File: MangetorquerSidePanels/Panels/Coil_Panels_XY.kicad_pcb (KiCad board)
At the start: 6 copper layers, 82 x 99 mm, 17 parts, among them J1 Through_Hole_1, J2 MOLEX_2053380006

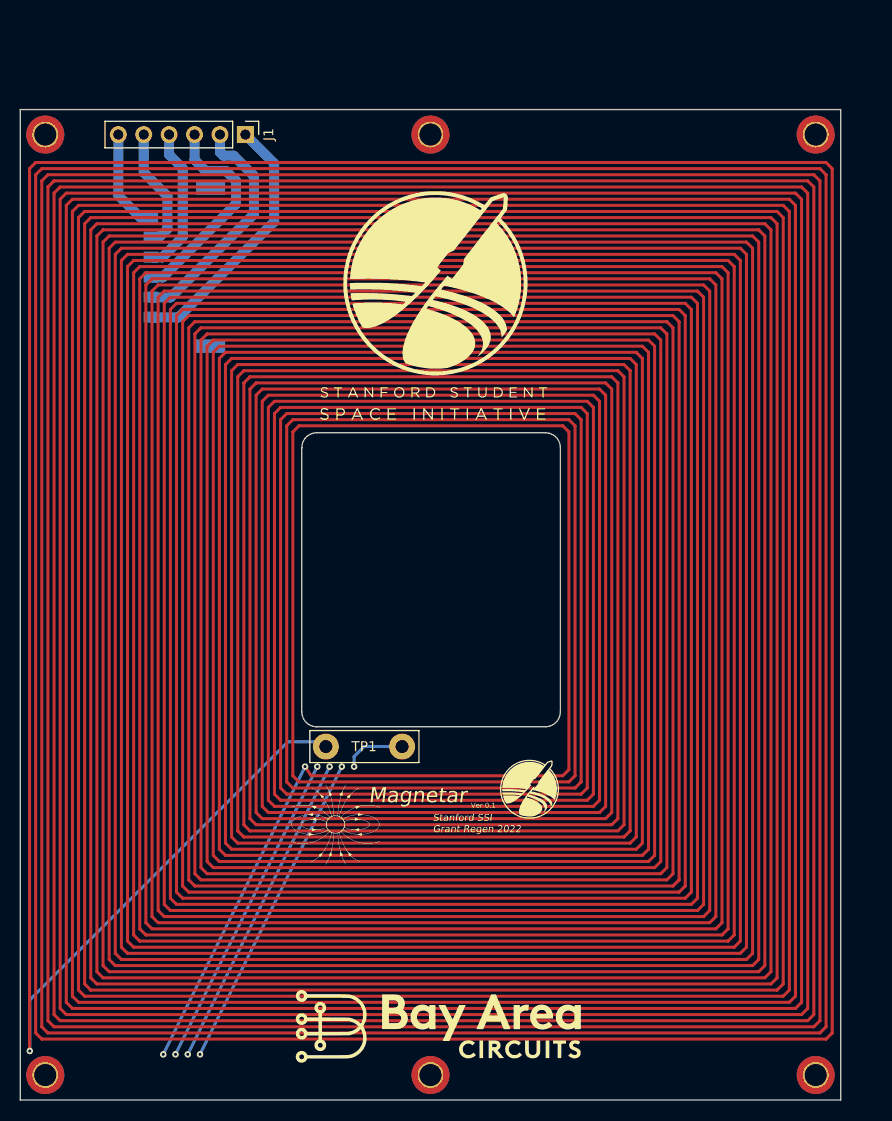
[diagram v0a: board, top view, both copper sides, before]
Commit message: Final flight side panels w/ magnetorquers finished, note final board thickness of 0.031'' and updated copper weight of 0.5oz for internal layers
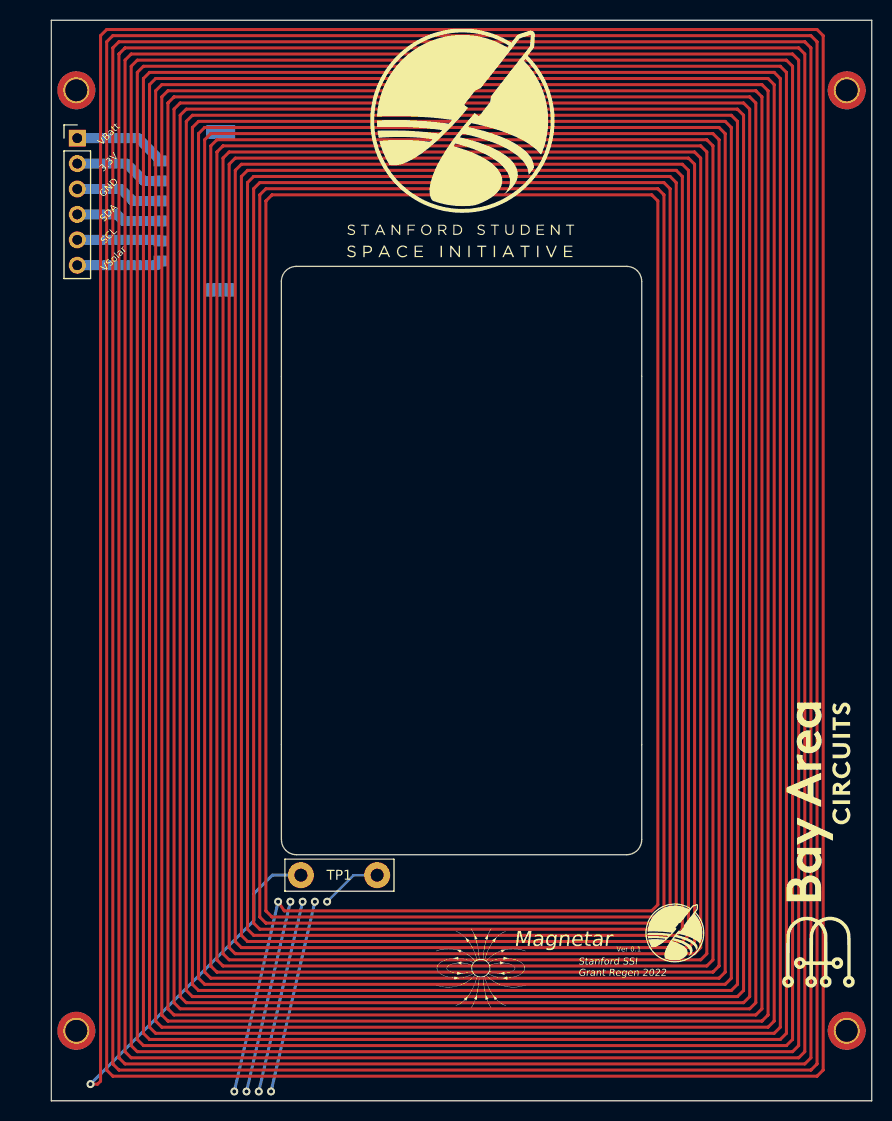
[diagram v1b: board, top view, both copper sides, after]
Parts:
- removed H5, H6: ~, MountingHole:MountingHole_2.2mm_M2_DIN965_Pad_TopBottom
- moved H2 98.8 mm to (192.0, 139.5)
- moved H4 98.5 mm to (115.0, 45.5)
- moved H1 89.6 mm to (115.0, 139.5)
- moved REF** 41.4 mm to (188.8, 120.7), turned to 90 degrees
- moved REF** 28.7 mm to (188.0, 130.5)
- moved REF** 28.7 mm to (168.7, 127.2)
- moved REF** 20.4 mm to (174.7, 130.0)
- moved REF** 20.4 mm to (155.5, 133.2)
- moved REF** 19.5 mm to (131.4, 137.0)
- moved J1 16.8 mm to (115.1, 50.3), turned to 0 degrees
- moved REF** 16.5 mm to (153.8, 49.2)
- moved REF** 15.9 mm to (153.4, 48.2)
- moved TP1 13.1 mm to (141.3, 124.4)
- moved J2 5.70 mm to (127.0, 57.6)
- moved H3 5.40 mm to (192.0, 45.5)
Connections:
- net Coil_OUT renamed Coil_IN
- J1 pad 1: Net-(J1-Pad1) -> Net-(J2-Pad1)
- J1 pad 2: Net-(J1-Pad2) -> Net-(J2-Pad2)
- J1 pad 3: Net-(J1-Pad3) -> Net-(J2-Pad3)
- J1 pad 4: Net-(J1-Pad4) -> Net-(J2-Pad4)
- J1 pad 5: Net-(J1-Pad5) -> Net-(J2-Pad5)
- J1 pad 6: Net-(J1-Pad6) -> Net-(J2-Pad6)
- J2 pad 1: Net-(J1-Pad6) -> Net-(J2-Pad1)
- J2 pad 2: Net-(J1-Pad5) -> Net-(J2-Pad2)
- J2 pad 3: Net-(J1-Pad4) -> Net-(J2-Pad3)
- J2 pad 4: Net-(J1-Pad3) -> Net-(J2-Pad4)
- J2 pad 5: Net-(J1-Pad2) -> Net-(J2-Pad5)
- J2 pad 6: Net-(J1-Pad1) -> Net-(J2-Pad6)
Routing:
- net Coil_IN: track 50604.5 -> 40226.0 mm
- net Net-(J1-Pad1): track 26.1 -> 0.00 mm
- net Net-(J1-Pad2): track 23.6 -> 0.00 mm
- net Net-(J1-Pad3): track 21.3 -> 0.00 mm
- net Net-(J1-Pad4): track 14.7 -> 0.00 mm
- net Net-(J1-Pad5): track 12.3 -> 0.00 mm
- net Net-(J1-Pad6): track 10.4 -> 0.00 mm
- net Net-(J2-Pad1): track 0.00 -> 9.30 mm
- net Net-(J2-Pad2): track 0.00 -> 9.08 mm
- net Net-(J2-Pad3): track 0.00 -> 8.86 mm
- net Net-(J2-Pad4): track 0.00 -> 8.63 mm
- net Net-(J2-Pad6): track 0.00 -> 8.54 mm
- net Net-(J2-Pad5): track 0.00 -> 8.41 mm
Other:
- board size 82 x 99 mm -> 82 x 108 mm
- board text added: "3.3V"
- board text added: "Thank you for all of your support Professor Elschot!"
- board text added: "Thank you to Professor Simone D'Amico for being an increadible advisor to our team and a caring mentor"
- board text added: "To my number one supporter, Beth Amos. Hopefully this one leaves the rocket :-) <3 Grant"
- board text added: "VBatt"
- board text added: "VSolar"
- board text added: "Vika+Clemens+Elian+Torin"
- board text removed: "3V3"
- board text removed: "VBATT"
- board text removed: "VSOLAR"

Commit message: added magnetorquers
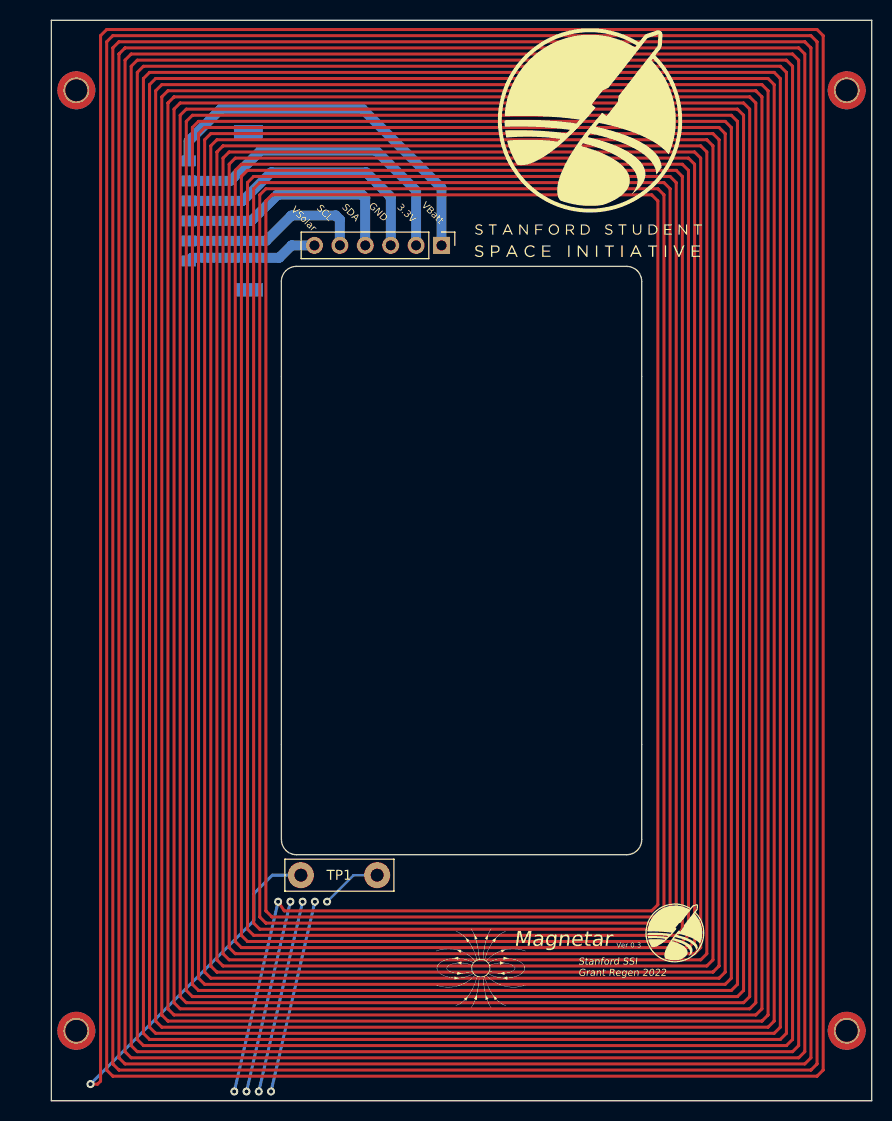
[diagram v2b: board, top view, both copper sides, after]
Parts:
- removed the REF** at (188.8, 120.7)
- moved J1 37.9 mm to (151.5, 61.0), turned to -90 degrees
- moved REF** 23.0 mm to (176.4, 48.2)
- moved REF** 12.8 mm to (166.6, 49.2)
- moved J2 2.77 mm to (129.8, 57.5)
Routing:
- net Net-(J2-Pad1): track 9.30 -> 37.6 mm
- net Net-(J2-Pad2): track 9.08 -> 31.1 mm
- net Net-(J2-Pad3): track 8.86 -> 27.2 mm
- net Net-(J2-Pad4): track 8.63 -> 23.6 mm
- net Net-(J2-Pad5): track 8.41 -> 18.9 mm
- net Net-(J2-Pad6): track 8.54 -> 13.2 mm
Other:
- board text added: "To my number one supporter, Beth Amos. Love you to the stars <3 Grant"
- board text added: "Ver 0.3"
- board text removed: "Thank you for all of your support Professor Elschot!"
- board text removed: "To my number one supporter, Beth Amos. Hopefully this one leaves the rocket :-) <3 Grant"
- board text removed: "Ver 0.1"
- board text removed: "Vika+Clemens+Elian+Torin"
